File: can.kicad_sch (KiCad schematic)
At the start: 8 parts, among them J1 PINHD_1x2_Male, U8 SN65HVD230

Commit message: begin layout
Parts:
- C19, C32, C33: footprint PCM_Capacitor_SMD_AKL:C_0402_1005Metric -> PCM_Capacitor_SMD_AKL:C_0603_1608Metric
- R1, R16: footprint PCM_Resistor_SMD_AKL:R_0402_1005Metric -> PCM_Resistor_SMD_AKL:R_0603_1608Metric
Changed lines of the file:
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@@
 			)
 		)
-		(property "Footprint" "PCM_Capacitor_SMD_AKL:C_0402_1005Metric"
+		(property "Footprint" "PCM_Capacitor_SMD_AKL:C_0603_1608Metric"
 			(at 171.45 97.79 0)
 			(effects
@@
 			)
 		)
-		(property "Datasheet" "~"
+		(property "Datasheet" ""
 			(at 171.45 97.79 0)
 			(effects
@@
 			)
 		)
-		(property "Footprint" "PCM_Resistor_SMD_AKL:R_0402_1005Metric"
+		(property "Footprint" "PCM_Resistor_SMD_AKL:R_0603_1608Metric"
 			(at 135.89 104.14 0)
 			(effects
@@
 			)
 		)
-		(property "Footprint" "PCM_Capacitor_SMD_AKL:C_0402_1005Metric"
+		(property "Footprint" "PCM_Capacitor_SMD_AKL:C_0603_1608Metric"
 			(at 171.45 118.11 0)
 			(effects
@@
 			)
 		)
-		(property "Datasheet" "~"
+		(property "Datasheet" ""
 			(at 171.45 118.11 0)
 			(effects
@@
 			)
 		)
-		(property "Footprint" "PCM_Capacitor_SMD_AKL:C_0402_1005Metric"
+		(property "Footprint" "PCM_Capacitor_SMD_AKL:C_0603_1608Metric"
 			(at 148.59 99.06 0)
 			(effects
@@
 			)
 		)
-		(property "Datasheet" "~"
+		(property "Datasheet" ""
 			(at 148.59 99.06 0)
 			(effects
@@
 			)
 		)
-		(property "Footprint" "PCM_Resistor_SMD_AKL:R_0402_1005Metric"
+		(property "Footprint" "PCM_Resistor_SMD_AKL:R_0603_1608Metric"
 			(at 161.798 104.14 90)
 			(effects
@@
 			)
 		)
-		(property "Datasheet" "~"
+		(property "Datasheet" ""
 			(at 160.02 104.14 0)
 			(effects

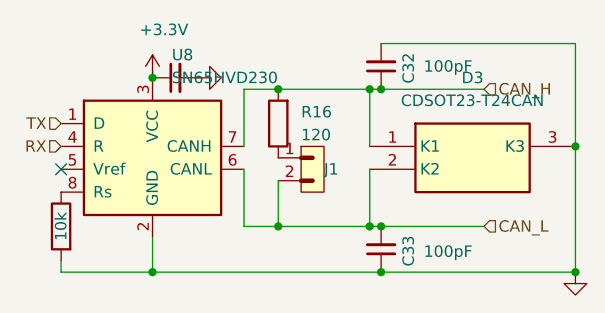
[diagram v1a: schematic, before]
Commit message: add cubemx project and redo some layour with new parts
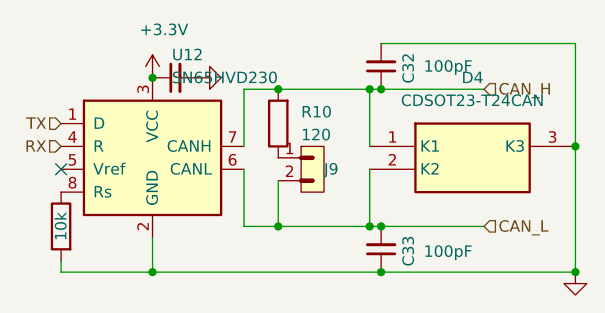
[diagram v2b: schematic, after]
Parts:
- renumbered C19 to C31, D3 to D4, J1 to J9, R16 to R10, R1 to R9, U8 to U12
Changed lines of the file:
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@@
 		(on_board yes)
 		(dnp no)
-		(property "Reference" "R1"
+		(property "Reference" "R9"
 			(at 133.35 115.57 90)
 			(effects
@@
 			(project "Active-Dampers"
 				(path "/81892b73-0b2d-4185-94d6-5966c81d614d/6235bd46-da8c-4baa-a7eb-9b733807c583"
-					(reference "R1")
+					(reference "R9")
 					(unit 1)
 				)
@@
 		(dnp no)
 		(fields_autoplaced yes)
-		(property "Reference" "#PWR06"
+		(property "Reference" "#PWR050"
 			(at 157.48 99.06 0)
 			(effects
@@
 			(project "Active-Dampers"
 				(path "/81892b73-0b2d-4185-94d6-5966c81d614d/6235bd46-da8c-4baa-a7eb-9b733807c583"
-					(reference "#PWR06")
+					(reference "#PWR050")
 					(unit 1)
 				)
@@
 		(on_board yes)
 		(dnp no)
-		(property "Reference" "C19"
+		(property "Reference" "C31"
 			(at 150.114 102.108 90)
 			(effects
@@
 			(project "Active-Dampers"
 				(path "/81892b73-0b2d-4185-94d6-5966c81d614d/6235bd46-da8c-4baa-a7eb-9b733807c583"
-					(reference "C19")
+					(reference "C31")
 					(unit 1)
 				)
@@
 		(dnp no)
 		(fields_autoplaced yes)
-		(property "Reference" "#PWR047"
+		(property "Reference" "#PWR051"
 			(at 193.04 127 0)
 			(effects
@@
 			(project "Active-Dampers"
 				(path "/81892b73-0b2d-4185-94d6-5966c81d614d/6235bd46-da8c-4baa-a7eb-9b733807c583"
-					(reference "#PWR047")
+					(reference "#PWR051")
 					(unit 1)
 				)
@@
 		(dnp no)
 		(fields_autoplaced yes)
-		(property "Reference" "U8"
+		(property "Reference" "U12"
 			(at 148.1933 96.52 0)
 			(effects
@@
 			(project ""
 				(path "/81892b73-0b2d-4185-94d6-5966c81d614d/6235bd46-da8c-4baa-a7eb-9b733807c583"
-					(reference "U8")
+					(reference "U12")
 					(unit 1)
 				)
@@
 		(on_board yes)
 		(dnp no)
-		(property "Reference" "#PWR07"
+		(property "Reference" "#PWR049"
 			(at 146.05 102.87 0)
 			(effects
@@
 			(project "Active-Dampers"
 				(path "/81892b73-0b2d-4185-94d6-5966c81d614d/6235bd46-da8c-4baa-a7eb-9b733807c583"
-					(reference "#PWR07")
+					(reference "#PWR049")
 					(unit 1)
 				)
@@
 		(dnp no)
 		(fields_autoplaced yes)
-		(property "Reference" "R16"
+		(property "Reference" "R10"
 			(at 162.56 102.8699 0)
 			(effects
@@
 		)
 		(property "Manufacturer_Part_Number" "AC0402FR-7D120RL"
+			(at 160.02 104.14 0)
+			(effects
+				(font
+					(size 1.27 1.27)
+				)
+				(hide yes)
+			)
+		)
+		(property "Current - Rectified" ""
+			(at 160.02 104.14 0)
+			(effects
+				(font
+					(size 1.27 1.27)
+				)
+				(hide yes)
+			)
+		)
+		(property "Height" ""
+			(at 160.02 104.14 0)
+			(effects
+				(font
+					(size 1.27 1.27)
+				)
+				(hide yes)
+			)
+		)
+		(property "Manufacturer_Name" ""
+			(at 160.02 104.14 0)
+			(effects
+				(font
+					(size 1.27 1.27)
+				)
+				(hide yes)
+			)
+		)
+		(property "Mouser Part Number" ""
+			(at 160.02 104.14 0)
+			(effects
+				(font
+					(size 1.27 1.27)
+				)
+				(hide yes)
+			)
+		)
+		(property "Mouser Price/Stock" ""
+			(at 160.02 104.14 0)
+			(effects
+				(font
+					(size 1.27 1.27)
+				)
+				(hide yes)
+			)
+		)
+		(property "Quiescent Current (Iq)" ""
+			(at 160.02 104.14 0)
+			(effects
+				(font
+					(size 1.27 1.27)
+				)
+				(hide yes)
+			)
+		)
+		(property "Voltage - DC Reverse(Vr)" ""
+			(at 160.02 104.14 0)
+			(effects
+				(font
+					(size 1.27 1.27)
+				)
+				(hide yes)
+			)
+		)
+		(property "Voltage - Forward(Vf@If)" ""
 			(at 160.02 104.14 0)
 			(effects
@@
 			(project "Active-Dampers"
 				(path "/81892b73-0b2d-4185-94d6-5966c81d614d/6235bd46-da8c-4baa-a7eb-9b733807c583"
-					(reference "R16")
+					(reference "R10")
 					(unit 1)
 				)
@@
 		(on_board yes)
 		(dnp no)
-		(property "Reference" "J1"
+		(property "Reference" "J9"
 			(at 165.1 109.22 0)
 			(effects
@@
 			(project ""
 				(path "/81892b73-0b2d-4185-94d6-5966c81d614d/6235bd46-da8c-4baa-a7eb-9b733807c583"
-					(reference "J1")
+					(reference "J9")
 					(unit 1)
 				)
@@
 		(dnp no)
 		(fields_autoplaced yes)
-		(property "Reference" "D3"
+		(property "Reference" "D4"
 			(at 181.61 99.06 0)
 			(effects
@@
 			(project "Active-Dampers"
 				(path "/81892b73-0b2d-4185-94d6-5966c81d614d/6235bd46-da8c-4baa-a7eb-9b733807c583"
-					(reference "D3")
+					(reference "D4")
 					(unit 1)
 				)
